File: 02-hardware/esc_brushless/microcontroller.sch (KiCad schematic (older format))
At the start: 18 parts

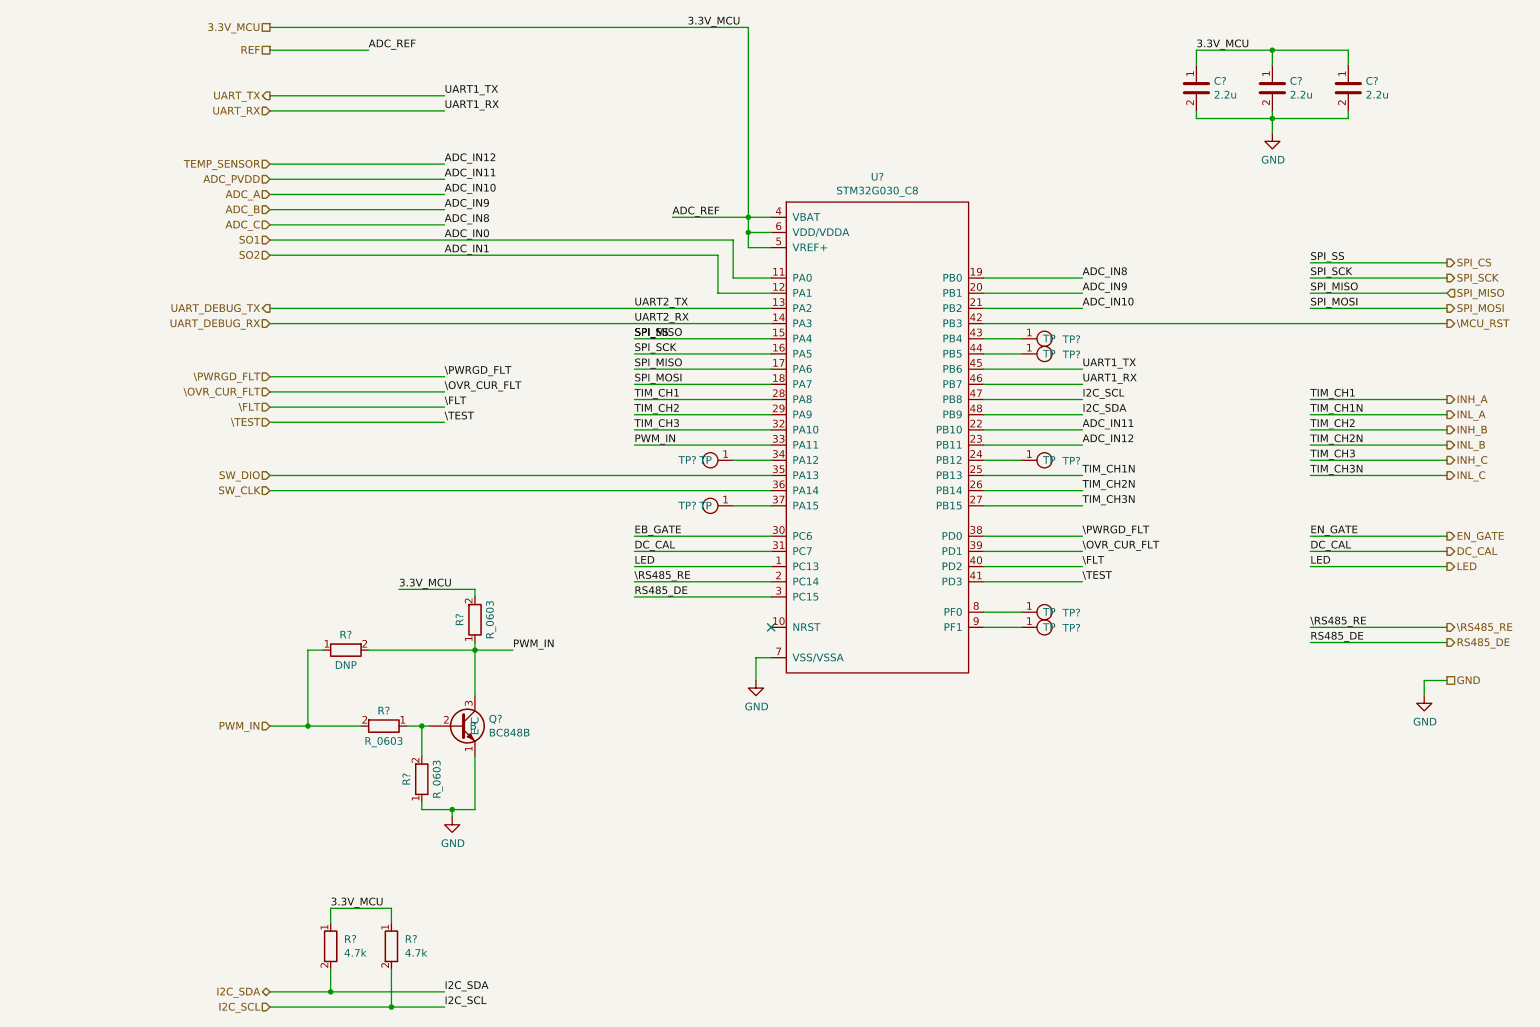
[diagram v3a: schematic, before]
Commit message: Schematics v1.0 - Fix DRC issues
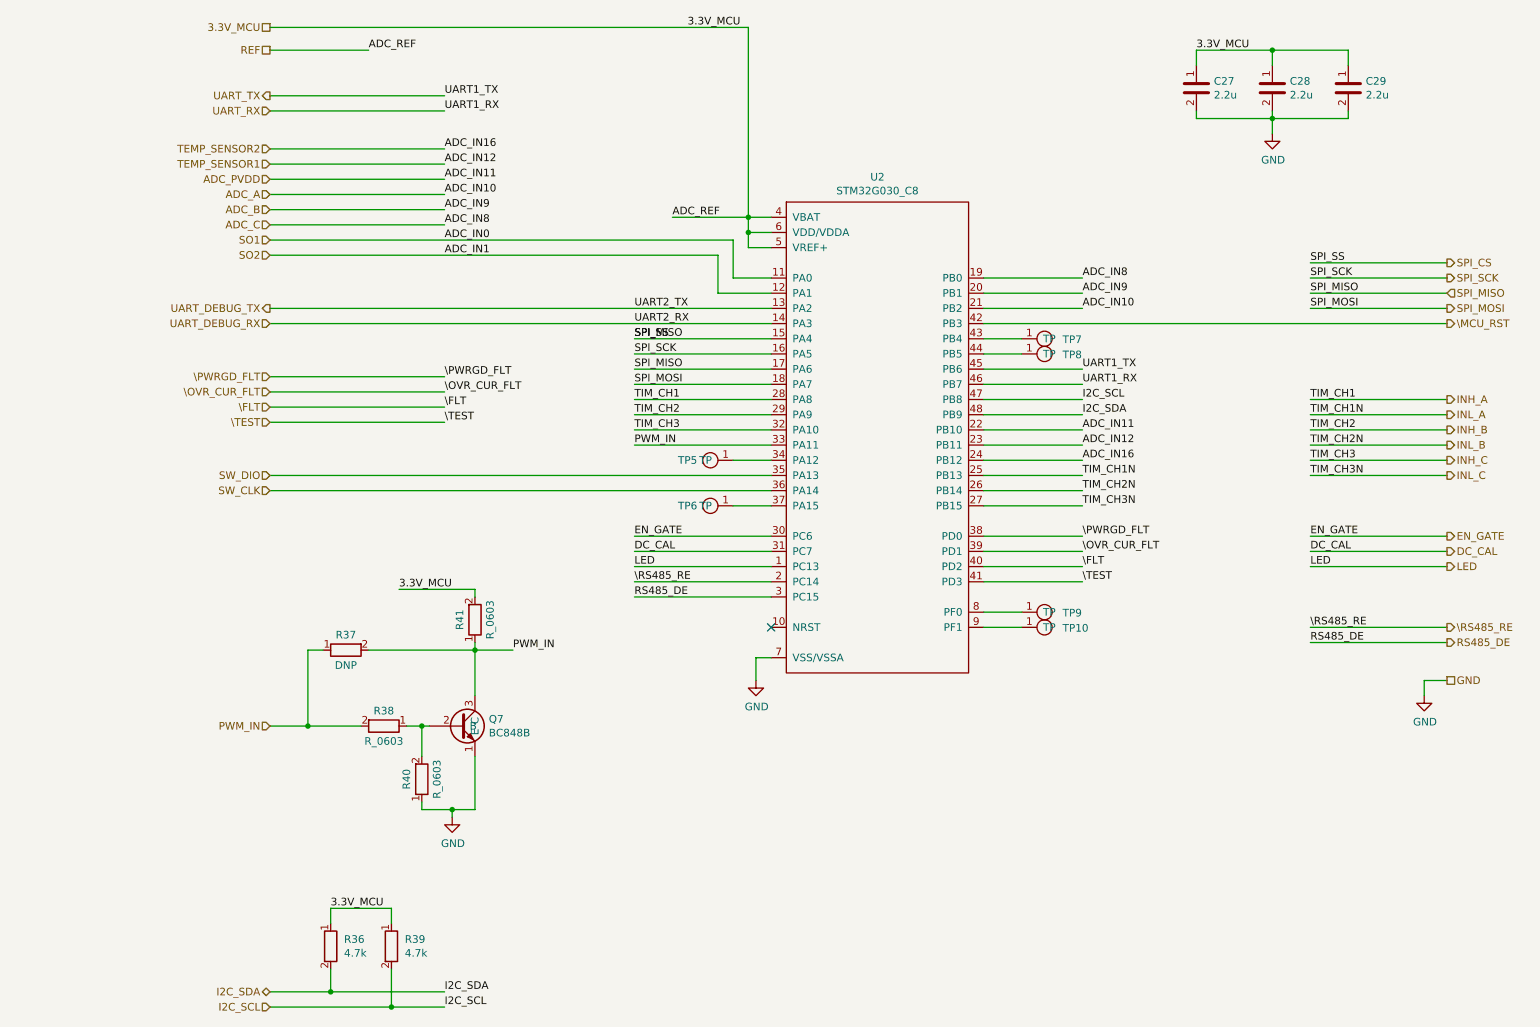
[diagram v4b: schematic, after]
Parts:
- removed TP?: test_point, p_Package_Misc:TP_SMD_1.25mm, symbol p_Misc:test_point
- gave numbers to parts that had none: 17
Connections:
- net EB_GATE is gone; now on net EN_GATE: U2.30 (PC6)
- net TEMP_SENSOR2: now reaches U2.24 (PB12)
- net TEMP_SENSOR renamed TEMP_SENSOR1
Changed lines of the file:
@@
 SW_DIO
 Text HLabel 2150 1800 0    50   Input ~ 0
-TEMP_SENSOR
+TEMP_SENSOR1
 Text HLabel 2150 1900 0    50   Input ~ 0
 ADC_PVDD
@@
 UART_TX
 $Comp
-L p_MCU:STM32G030_C8 U?
+L p_MCU:STM32G030_C8 U2
 U 1 1 607AAEF6
 P 6150 3600
-F 0 "U?" H 6150 5315 50  0000 C CNN
+F 0 "U2" H 6150 5315 50  0000 C CNN
 F 1 "STM32G030_C8" H 6150 5224 50  0000 C CNN
 F 2 "p_Package_QFP:LQFP-48_7x7mm_P0.5mm" H 6250 1950 50  0001 C CNN
@@
 	5300 2150 5450 2150
 $Comp
-L p_Passive:C_0603 C?
+L p_Passive:C_0603 C27
 U 1 1 607AE35E
 P 8250 1300
-F 0 "C?" H 8365 1346 50  0000 L CNN
+F 0 "C27" H 8365 1346 50  0000 L CNN
 F 1 "2.2u" H 8365 1255 50  0000 L CNN
 F 2 "p_Package_Capacitor_SMD:C_0603_1608Metric_Pad1.08x0.95mm_HandSolder" H 8250 1300 50  0001 C CNN
@@
 $EndComp
 $Comp
-L p_Passive:C_0603 C?
+L p_Passive:C_0603 C28
 U 1 1 607AE9BE
 P 8750 1300
-F 0 "C?" H 8865 1346 50  0000 L CNN
+F 0 "C28" H 8865 1346 50  0000 L CNN
 F 1 "2.2u" H 8865 1255 50  0000 L CNN
 F 2 "p_Package_Capacitor_SMD:C_0603_1608Metric_Pad1.08x0.95mm_HandSolder" H 8750 1300 50  0001 C CNN
@@
 $EndComp
 $Comp
-L p_Passive:C_0603 C?
+L p_Passive:C_0603 C29
 U 1 1 607AECD1
 P 9250 1300
-F 0 "C?" H 9365 1346 50  0000 L CNN
+F 0 "C29" H 9365 1346 50  0000 L CNN
 F 1 "2.2u" H 9365 1255 50  0000 L CNN
 F 2 "p_Package_Capacitor_SMD:C_0603_1608Metric_Pad1.08x0.95mm_HandSolder" H 9250 1300 50  0001 C CNN
@@
 	9250 1050 8750 1050
 $Comp
-L power:GND #PWR?
+L power:GND #PWR044
 U 1 1 607C423E
 P 8750 1600
-F 0 "#PWR?" H 8750 1350 50  0001 C CNN
+F 0 "#PWR044" H 8750 1350 50  0001 C CNN
 F 1 "GND" H 8755 1427 50  0000 C CNN
 F 2 "" H 8750 1600 50  0001 C CNN
@@
 $EndComp
 $Comp
-L power:GND #PWR?
+L power:GND #PWR043
 U 1 1 607C5BA3
 P 5350 5200
-F 0 "#PWR?" H 5350 4950 50  0001 C CNN
+F 0 "#PWR043" H 5350 4950 50  0001 C CNN
 F 1 "GND" H 5355 5027 50  0000 C CNN
 F 2 "" H 5350 5200 50  0001 C CNN
@@
 I2C_SCL
 $Comp
-L p_Passive:R_0603 R?
+L p_Passive:R_0603 R36
 U 1 1 607D2E69
 P 2550 6950
-F 0 "R?" H 2638 6996 50  0000 L CNN
+F 0 "R36" H 2638 6996 50  0000 L CNN
 F 1 "4.7k" H 2638 6905 50  0000 L CNN
 F 2 "p_Package_Resistor_SMD:R_0603_1608Metric_Pad0.98x0.95mm_HandSolder" H 2550 6950 50  0001 C CNN
@@
 $EndComp
 $Comp
-L p_Passive:R_0603 R?
+L p_Passive:R_0603 R39
 U 1 1 607D3692
 P 2950 6950
-F 0 "R?" H 3038 6996 50  0000 L CNN
+F 0 "R39" H 3038 6996 50  0000 L CNN
 F 1 "4.7k" H 3038 6905 50  0000 L CNN
 F 2 "p_Package_Resistor_SMD:R_0603_1608Metric_Pad0.98x0.95mm_HandSolder" H 2950 6950 50  0001 C CNN
@@
 	4550 4650 5450 4650
 Text Label 4550 4250 0    50   ~ 0
-EB_GATE
+EN_GATE
 Text Label 4550 4350 0    50   ~ 0
 DC_CAL
@@
 RS485_DE
 $Comp
-L p_Transistor_bipolar:BC848B Q?
+L p_Transistor_bipolar:BC848B Q7
 U 1 1 60949F59
 P 3500 5500
-F 0 "Q?" H 3591 5546 50  0000 L CNN
+F 0 "Q7" H 3591 5546 50  0000 L CNN
 F 1 "BC848B" H 3591 5455 50  0000 L CNN
 F 2 "p_Package_SOT:SOT-23" H 3500 5200 50  0001 C CNN
@@
 $EndComp
 $Comp
-L power:GND #PWR?
+L power:GND #PWR042
 U 1 1 6094AB0F
 P 3350 6100
-F 0 "#PWR?" H 3350 5850 50  0001 C CNN
+F 0 "#PWR042" H 3350 5850 50  0001 C CNN
 F 1 "GND" H 3355 5927 50  0000 C CNN
 F 2 "" H 3350 6100 50  0001 C CNN
@@
 3.3V_MCU
 $Comp
-L p_Passive:R_0603 R?
+L p_Passive:R_0603 R38
 U 1 1 60964833
 P 2900 5500
-F 0 "R?" V 2800 5500 50  0000 C CNN
+F 0 "R38" V 2800 5500 50  0000 C CNN
 F 1 "R_0603" V 3000 5500 50  0000 C CNN
 F 2 "p_Package_Resistor_SMD:R_0603_1608Metric_Pad0.98x0.95mm_HandSolder" H 2900 5500 50  0001 C CNN
@@
 $EndComp
 $Comp
-L p_Passive:R_0603 R?
+L p_Passive:R_0603 R40
 U 1 1 6096D73F
 P 3150 5850
-F 0 "R?" V 3050 5850 50  0000 C CNN
+F 0 "R40" V 3050 5850 50  0000 C CNN
 F 1 "R_0603" V 3250 5850 50  0000 C CNN
 F 2 "p_Package_Resistor_SMD:R_0603_1608Metric_Pad0.98x0.95mm_HandSolder" H 3150 5850 50  0001 C CNN
@@
 $EndComp
 $Comp
-L p_Passive:R_0603 R?
+L p_Passive:R_0603 R41
 U 1 1 6098DB94
 P 3500 4800
-F 0 "R?" V 3400 4800 50  0000 C CNN
+F 0 "R41" V 3400 4800 50  0000 C CNN
 F 1 "R_0603" V 3600 4800 50  0000 C CNN
 F 2 "p_Package_Resistor_SMD:R_0603_1608Metric_Pad0.98x0.95mm_HandSolder" H 3500 4800 50  0001 C CNN
@@
 PWM_IN
 $Comp
-L p_Passive:R_0603 R?
+L p_Passive:R_0603 R37
 U 1 1 6087455B
 P 2650 5000
-F 0 "R?" V 2550 5000 50  0000 C CNN
+F 0 "R37" V 2550 5000 50  0000 C CNN
 F 1 "DNP" V 2750 5000 50  0000 C CNN
 F 2 "p_Package_Resistor_SMD:R_0603_1608Metric_Pad0.98x0.95mm_HandSolder" H 2650 5000 50  0001 C CNN
@@
 GND
 $Comp
-L power:GND #PWR?
+L power:GND #PWR045
 U 1 1 608C887C
 P 9750 5300
-F 0 "#PWR?" H 9750 5050 50  0001 C CNN
+F 0 "#PWR045" H 9750 5050 50  0001 C CNN
 F 1 "GND" H 9755 5127 50  0000 C CNN
 F 2 "" H 9750 5300 50  0001 C CNN
@@
 	9750 5200 9750 5300
 $Comp
-L p_Misc:test_point TP?
+L p_Misc:test_point TP9
 U 1 1 608CEC2C
 P 7200 4750
-F 0 "TP?" H 7031 4755 50  0000 R CNN
+F 0 "TP9" H 7031 4755 50  0000 R CNN
 F 1 "test_point" H 7187 4884 50  0001 C CNN
 F 2 "p_Package_Misc:TP_SMD_1.25mm" H 7200 4550 50  0001 C CNN
@@
 $EndComp
 $Comp
-L p_Misc:test_point TP?
+L p_Misc:test_point TP10
 U 1 1 608DA935
 P 7200 4850
-F 0 "TP?" H 7031 4855 50  0000 R CNN
+F 0 "TP10" H 7031 4855 50  0000 R CNN
 F 1 "test_point" H 7187 4984 50  0001 C CNN
 F 2 "p_Package_Misc:TP_SMD_1.25mm" H 7200 4650 50  0001 C CNN
@@
 	6850 4850 7100 4850
 $Comp
-L p_Misc:test_point TP?
+L p_Misc:test_point TP6
 U 1 1 608E544E
 P 5100 4050
-F 0 "TP?" H 4900 4050 50  0000 C CNN
+F 0 "TP6" H 4900 4050 50  0000 C CNN
 F 1 "test_point" H 5087 4184 50  0001 C CNN
 F 2 "p_Package_Misc:TP_SMD_1.25mm" H 5100 3850 50  0001 C CNN
@@
 	5200 4050 5450 4050
 $Comp
-L p_Misc:test_point TP?
+L p_Misc:test_point TP5
 U 1 1 609117C2
 P 5100 3750
-F 0 "TP?" H 4900 3750 50  0000 C CNN
+F 0 "TP5" H 4900 3750 50  0000 C CNN
 F 1 "test_point" H 5087 3884 50  0001 C CNN
 F 2 "p_Package_Misc:TP_SMD_1.25mm" H 5100 3550 50  0001 C CNN
@@
 	5200 3750 5450 3750
 $Comp
-L p_Misc:test_point TP?
-U 1 1 60917464
-P 7200 3750
-F 0 "TP?" H 7031 3755 50  0000 R CNN
-F 1 "test_point" H 7187 3884 50  0001 C CNN
-F 2 "p_Package_Misc:TP_SMD_1.25mm" H 7200 3550 50  0001 C CNN
-F 3 "" H 7200 3750 50  0001 C CNN
-	1    7200 3750
-	-1   0    0    1
-$EndComp
-$Comp
-L p_Misc:test_point TP?
+L p_Misc:test_point TP8
 U 1 1 60917A46
 P 7200 3050
-F 0 "TP?" H 7031 3055 50  0000 R CNN
+F 0 "TP8" H 7031 3055 50  0000 R CNN
 F 1 "test_point" H 7187 3184 50  0001 C CNN
 F 2 "p_Package_Misc:TP_SMD_1.25mm" H 7200 2850 50  0001 C CNN
@@
 $EndComp
 $Comp
-L p_Misc:test_point TP?
+L p_Misc:test_point TP7
 U 1 1 60917D91
 P 7200 2950
-F 0 "TP?" H 7031 2955 50  0000 R CNN
+F 0 "TP7" H 7031 2955 50  0000 R CNN
 F 1 "test_point" H 7187 3084 50  0001 C CNN
 F 2 "p_Package_Misc:TP_SMD_1.25mm" H 7200 2750 50  0001 C CNN
@@
 Wire Wire Line
 	6850 2950 7100 2950
-Wire Wire Line
-	6850 3750 7100 3750
 NoConn ~ 5450 4850
+Wire Wire Line
+	6850 3750 7500 3750
+Text Label 7500 3750 0    50   ~ 0
+ADC_IN16
+Text HLabel 2150 1700 0    50   Input ~ 0
+TEMP_SENSOR2
+Wire Wire Line
+	2150 1700 3300 1700
+Text Label 3300 1700 0    50   ~ 0
+ADC_IN16
 $EndSCHEMATC

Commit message: Schematics v1.0 - Remove some options and test points
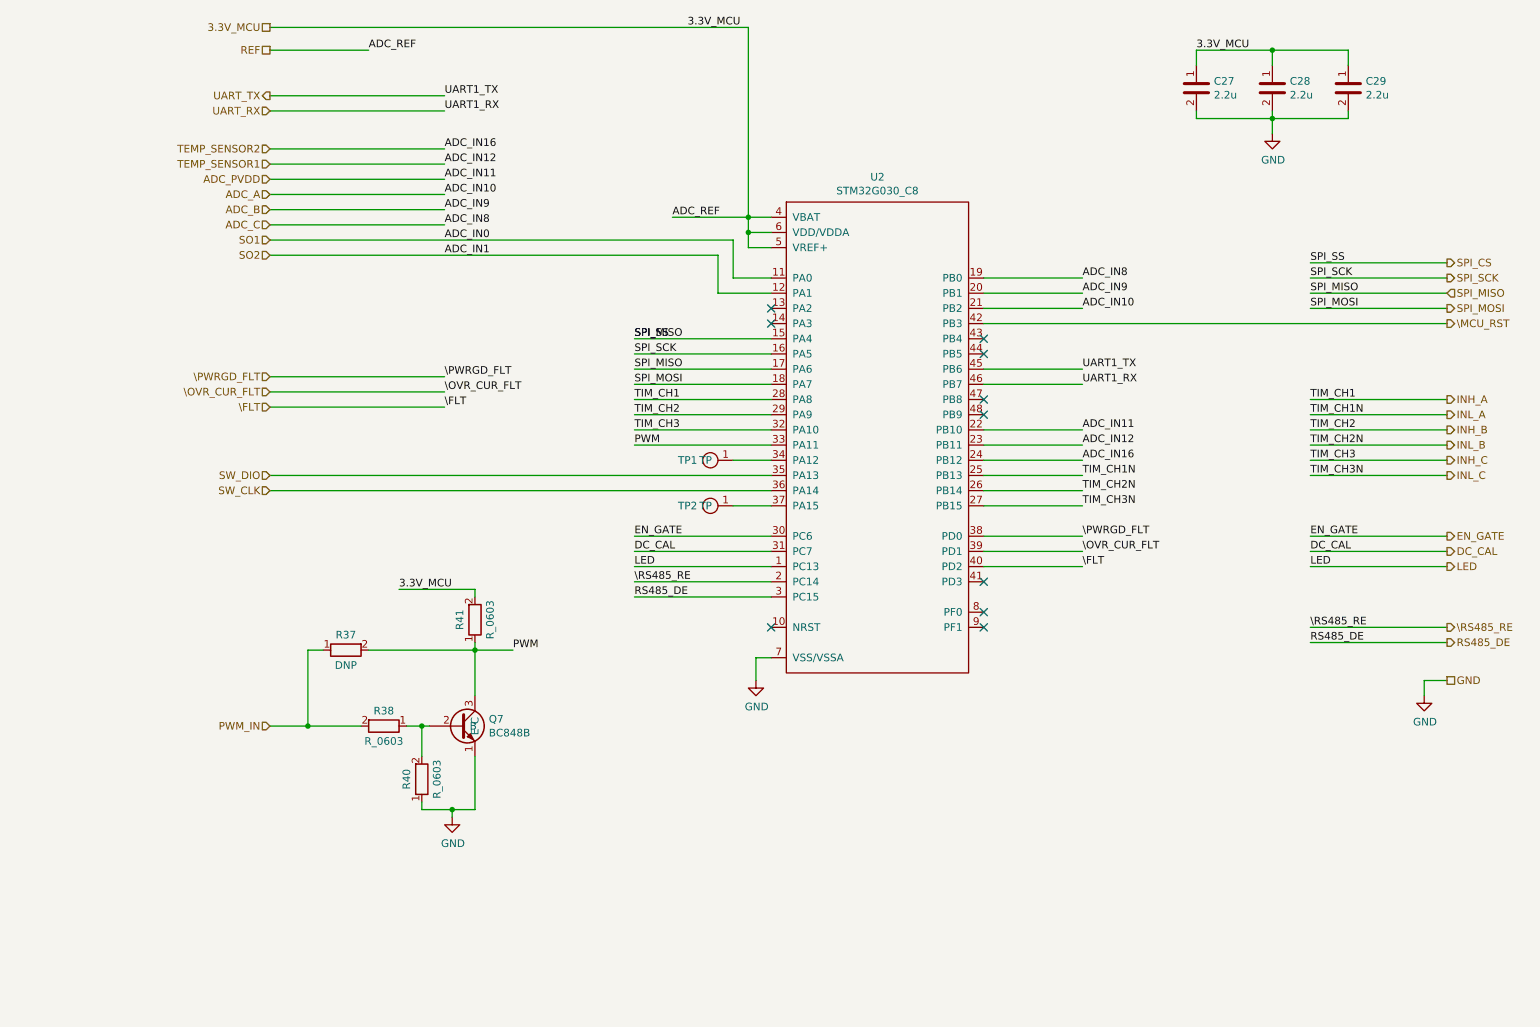
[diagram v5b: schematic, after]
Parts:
- removed R36, R39: 4.7k, p_Package_Resistor_SMD:R_0603_1608Metric_Pad0.98x0.95mm_HandSolder, symbol p_Passive:R_0603
- removed TP10, TP7, TP8, TP9: test_point, p_Package_Misc:TP_SMD_1.25mm, symbol p_Misc:test_point
- renumbered TP5 to TP1, TP6 to TP2
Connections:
- net PWM_IN: no longer Q7.3 (C), R37.2, R41.1, U2.33 (PA11)
- net I2C_SCL: no longer names the net of U2.47 (PB8)
- net I2C_SDA: no longer names the net of U2.48 (PB9)
- net UART_DEBUG_RX: no longer names the net of U2.14 (PA3)
- net UART_DEBUG_TX: no longer names the net of U2.13 (PA2)
- net \TEST: no longer names the net of U2.41 (PD3)
- new net PWM: Q7.3 (C), R37.2, R41.1, U2.33 (PA11)
- no-connect marks 1 -> 10
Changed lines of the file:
@@
 Text HLabel 2150 1450 0    50   Input ~ 0
 UART_RX
-Text HLabel 2150 7250 0    50   BiDi ~ 0
-I2C_SDA
-Text HLabel 2150 7350 0    50   Input ~ 0
-I2C_SCL
 Text HLabel 2150 3950 0    50   Input ~ 0
 SW_CLK
@@
 Text HLabel 9900 4450 2    50   Output ~ 0
 LED
-Text HLabel 2150 3500 0    50   Input ~ 0
-\TEST
-Text HLabel 2150 2750 0    50   Output ~ 0
-UART_DEBUG_TX
-Text HLabel 2150 2850 0    50   Input ~ 0
-UART_DEBUG_RX
 Text HLabel 9900 4850 2    50   Output ~ 0
 \RS485_RE
@@
 Text Label 4900 900  0    50   ~ 0
 3.3V_MCU
-Text Label 3300 7250 0    50   ~ 0
-I2C_SDA
-Text Label 3300 7350 0    50   ~ 0
-I2C_SCL
-Wire Wire Line
-	6850 3350 7500 3350
-Wire Wire Line
-	6850 3450 7500 3450
-Text Label 7500 3450 0    50   ~ 0
-I2C_SDA
-Text Label 7500 3350 0    50   ~ 0
-I2C_SCL
-$Comp
-L p_Passive:R_0603 R36
-U 1 1 607D2E69
-P 2550 6950
-F 0 "R36" H 2638 6996 50  0000 L CNN
-F 1 "4.7k" H 2638 6905 50  0000 L CNN
-F 2 "p_Package_Resistor_SMD:R_0603_1608Metric_Pad0.98x0.95mm_HandSolder" H 2550 6950 50  0001 C CNN
-F 3 "" H 2550 6950 50  0001 C CNN
-	1    2550 6950
-	1    0    0    -1
-$EndComp
-$Comp
-L p_Passive:R_0603 R39
-U 1 1 607D3692
-P 2950 6950
-F 0 "R39" H 3038 6996 50  0000 L CNN
-F 1 "4.7k" H 3038 6905 50  0000 L CNN
-F 2 "p_Package_Resistor_SMD:R_0603_1608Metric_Pad0.98x0.95mm_HandSolder" H 2950 6950 50  0001 C CNN
-F 3 "" H 2950 6950 50  0001 C CNN
-	1    2950 6950
-	1    0    0    -1
-$EndComp
-Wire Wire Line
-	2950 6800 2950 6700
-Wire Wire Line
-	2950 6700 2550 6700
-Wire Wire Line
-	2550 6700 2550 6800
-Text Label 2550 6700 0    50   ~ 0
-3.3V_MCU
-Wire Wire Line
-	2150 7250 2550 7250
-Wire Wire Line
-	2150 7350 2950 7350
-Wire Wire Line
-	2550 7100 2550 7250
-Connection ~ 2550 7250
-Wire Wire Line
-	2550 7250 3300 7250
-Wire Wire Line
-	2950 7100 2950 7350
-Connection ~ 2950 7350
-Wire Wire Line
-	2950 7350 3300 7350
 Wire Wire Line
 	6850 3150 7500 3150
@@
 Text Label 7500 3250 0    50   ~ 0
 UART1_RX
-Text Label 7500 3150 0    50   ~ 0
-UART1_TX
 Wire Wire Line
 	2150 1450 3300 1450
@@
 Text Label 4550 2950 0    50   ~ 0
 SPI_MISO
-Text Label 4550 2750 0    50   ~ 0
-UART2_TX
-Text Label 4550 2850 0    50   ~ 0
-UART2_RX
-Wire Wire Line
-	2150 2750 5450 2750
-Wire Wire Line
-	2150 2850 5450 2850
 Wire Wire Line
 	6850 3850 7500 3850
@@
 ADC_REF
 Wire Wire Line
-	2150 3500 3300 3500
-Text Label 3300 3500 0    50   ~ 0
-\TEST
-Wire Wire Line
 	2150 3400 3300 3400
 Wire Wire Line
@@
 Text Label 7500 4450 0    50   ~ 0
 \FLT
-Wire Wire Line
-	6850 4550 7500 4550
-Text Label 7500 4550 0    50   ~ 0
-\TEST
 Text Label 9000 4250 0    50   ~ 0
 EN_GATE
@@
 	9000 4950 9900 4950
 Text Label 4550 3650 0    50   ~ 0
-PWM_IN
+PWM
 Wire Wire Line
 	4550 3650 5450 3650
@@
 PWM_IN
 Text Label 3750 5000 0    50   ~ 0
-PWM_IN
+PWM
 $Comp
 L p_Passive:R_0603 R37
@@
 	9750 5200 9750 5300
 $Comp
-L p_Misc:test_point TP9
-U 1 1 608CEC2C
-P 7200 4750
-F 0 "TP9" H 7031 4755 50  0000 R CNN
-F 1 "test_point" H 7187 4884 50  0001 C CNN
-F 2 "p_Package_Misc:TP_SMD_1.25mm" H 7200 4550 50  0001 C CNN
-F 3 "" H 7200 4750 50  0001 C CNN
-	1    7200 4750
-	-1   0    0    1
-$EndComp
-$Comp
-L p_Misc:test_point TP10
-U 1 1 608DA935
-P 7200 4850
-F 0 "TP10" H 7031 4855 50  0000 R CNN
-F 1 "test_point" H 7187 4984 50  0001 C CNN
-F 2 "p_Package_Misc:TP_SMD_1.25mm" H 7200 4650 50  0001 C CNN
-F 3 "" H 7200 4850 50  0001 C CNN
-	1    7200 4850
-	-1   0    0    1
-$EndComp
-Wire Wire Line
-	6850 4750 7100 4750
-Wire Wire Line
-	6850 4850 7100 4850
-$Comp
-L p_Misc:test_point TP6
+L p_Misc:test_point TP2
 U 1 1 608E544E
 P 5100 4050
-F 0 "TP6" H 4900 4050 50  0000 C CNN
+F 0 "TP2" H 4900 4050 50  0000 C CNN
 F 1 "test_point" H 5087 4184 50  0001 C CNN
 F 2 "p_Package_Misc:TP_SMD_1.25mm" H 5100 3850 50  0001 C CNN
@@
 	5200 4050 5450 4050
 $Comp
-L p_Misc:test_point TP5
+L p_Misc:test_point TP1
 U 1 1 609117C2
 P 5100 3750
-F 0 "TP5" H 4900 3750 50  0000 C CNN
+F 0 "TP1" H 4900 3750 50  0000 C CNN
 F 1 "test_point" H 5087 3884 50  0001 C CNN
 F 2 "p_Package_Misc:TP_SMD_1.25mm" H 5100 3550 50  0001 C CNN
@@
 Wire Wire Line
 	5200 3750 5450 3750
-$Comp
-L p_Misc:test_point TP8
-U 1 1 60917A46
-P 7200 3050
-F 0 "TP8" H 7031 3055 50  0000 R CNN
-F 1 "test_point" H 7187 3184 50  0001 C CNN
-F 2 "p_Package_Misc:TP_SMD_1.25mm" H 7200 2850 50  0001 C CNN
-F 3 "" H 7200 3050 50  0001 C CNN
-	1    7200 3050
-	-1   0    0    1
-$EndComp
-$Comp
-L p_Misc:test_point TP7
-U 1 1 60917D91
-P 7200 2950
-F 0 "TP7" H 7031 2955 50  0000 R CNN
-F 1 "test_point" H 7187 3084 50  0001 C CNN
-F 2 "p_Package_Misc:TP_SMD_1.25mm" H 7200 2750 50  0001 C CNN
-F 3 "" H 7200 2950 50  0001 C CNN
-	1    7200 2950
-	-1   0    0    1
-$EndComp
-Wire Wire Line
-	6850 3050 7100 3050
-Wire Wire Line
-	6850 2950 7100 2950
 NoConn ~ 5450 4850
 Wire Wire Line
@@
 Text Label 3300 1700 0    50   ~ 0
 ADC_IN16
+NoConn ~ 6850 4550
+NoConn ~ 6850 4750
+NoConn ~ 6850 4850
+NoConn ~ 5450 2750
+NoConn ~ 5450 2850
+Text Label 7500 3150 0    50   ~ 0
+UART1_TX
+NoConn ~ 6850 2950
+NoConn ~ 6850 3050
+NoConn ~ 6850 3350
+NoConn ~ 6850 3450
 $EndSCHEMATC
